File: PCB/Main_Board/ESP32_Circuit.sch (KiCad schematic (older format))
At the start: 24 parts, among them Q1 MBT3904DW1, SW2 EN, SW3 BOOT, U2 ESP32-WROOM-32, U3 FT231XS

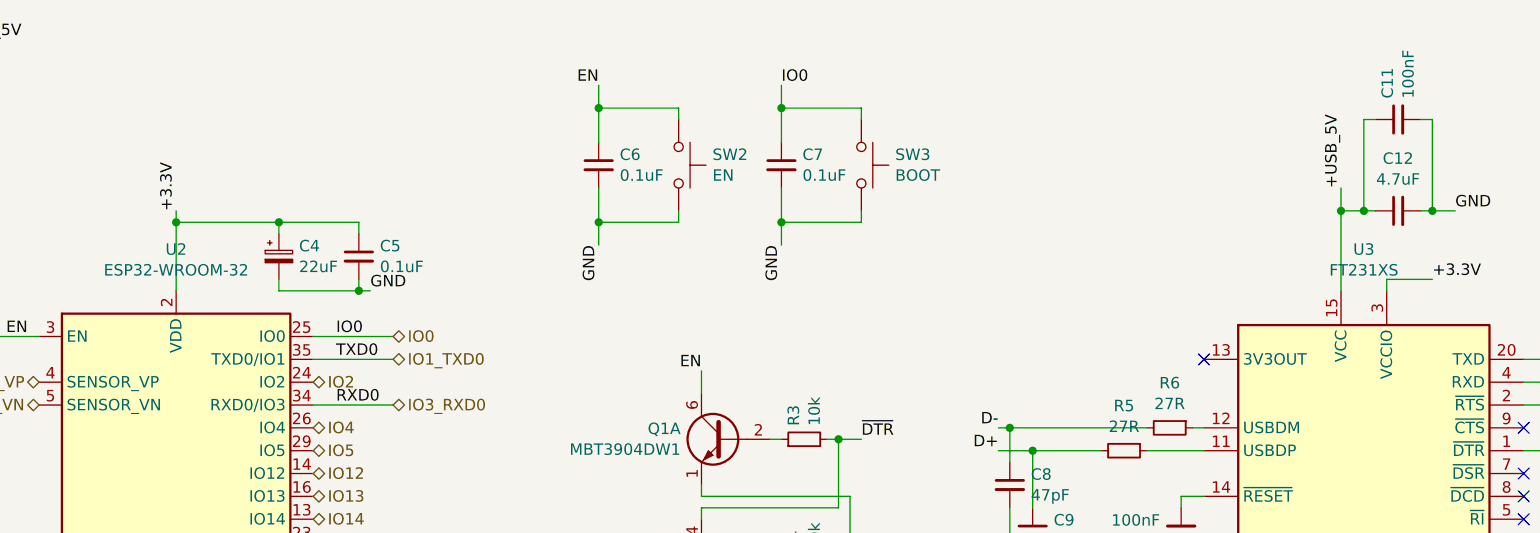
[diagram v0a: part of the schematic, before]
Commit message: Add IR circuit
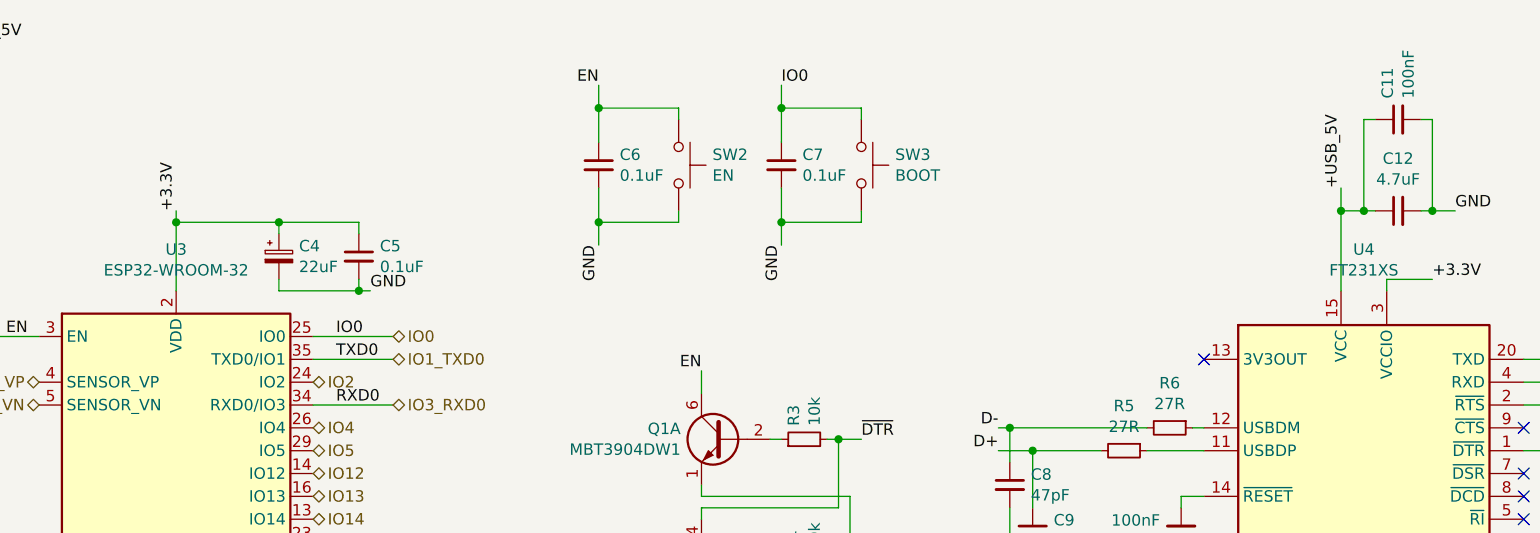
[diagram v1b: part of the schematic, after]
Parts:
- renumbered U2 to U3, U3 to U4
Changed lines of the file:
@@
 AR Path="/5F5D60CE" Ref="U?"  Part="1"
 AR Path="/5F591C5D/5F5D60CE" Ref="U?"  Part="1"
-AR Path="/5F889015/5F5D60CE" Ref="U3"  Part="1"
-F 0 "U3" H 8300 4731 50  0000 C CNN
+AR Path="/5F889015/5F5D60CE" Ref="U4"  Part="1"
+F 0 "U4" H 8300 4731 50  0000 C CNN
 F 1 "FT231XS" H 8300 4640 50  0000 C CNN
 F 2 "Package_SO:SSOP-20_3.9x8.7mm_P0.635mm" H 9300 2850 50  0001 C CNN
@@
 AR Path="/5F5F2511" Ref="U?"  Part="1"
 AR Path="/5F591C5D/5F5F2511" Ref="U?"  Part="1"
-AR Path="/5F889015/5F5F2511" Ref="U2"  Part="1"
-F 0 "U2" H 3100 5731 50  0000 C CNN
+AR Path="/5F889015/5F5F2511" Ref="U3"  Part="1"
+F 0 "U3" H 3100 5731 50  0000 C CNN
 F 1 "ESP32-WROOM-32" H 3100 5640 50  0000 C CNN
 F 2 "RF_Module:ESP32-WROOM-32" H 3100 2650 50  0001 C CNN

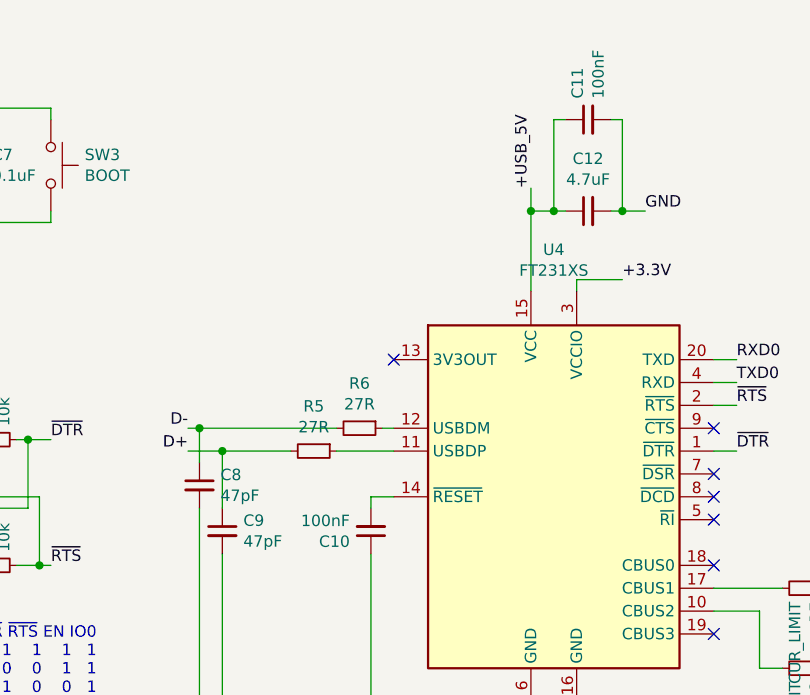
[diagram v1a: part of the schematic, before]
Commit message: Further schematic work and footprint association
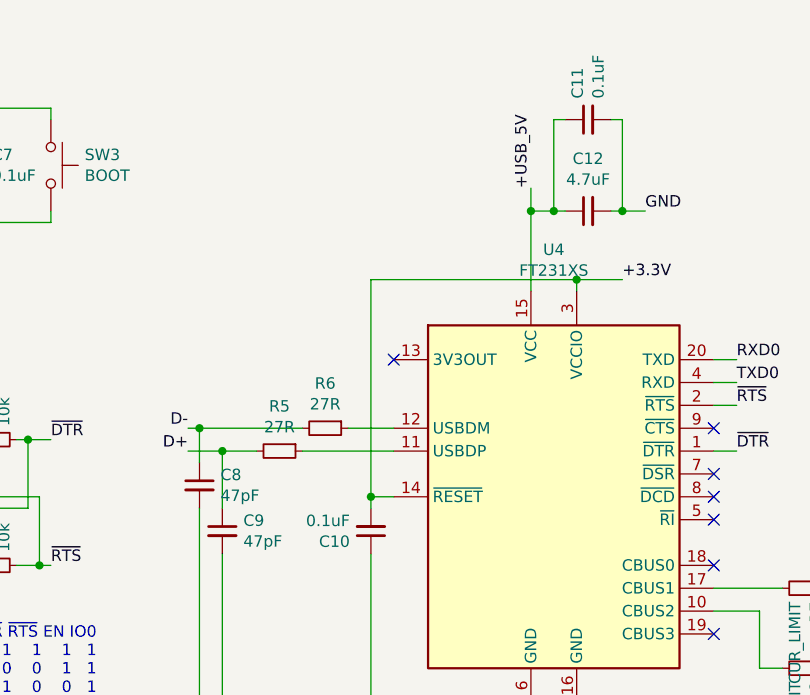
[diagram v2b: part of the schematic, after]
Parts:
- C10, C11: value 100nF -> 0.1uF; footprint (none) -> Capacitor_SMD:C_0603_1608Metric_Pad1.05x0.95mm_HandSolder
- C12, C3, C4, C5, C6, C7, C8, C9: footprint (none) -> Capacitor_SMD:C_0603_1608Metric_Pad1.05x0.95mm_HandSolder
- D5, D6: footprint (none) -> LED_SMD:LED_0603_1608Metric_Pad1.05x0.95mm_HandSolder
- R2, R3, R4, R5, R6, R7, R8: footprint (none) -> Resistor_SMD:R_0603_1608Metric_Pad1.05x0.95mm_HandSolder
- SW2, SW3: footprint (none) -> Button_Switch_THT:SW_PUSH_6mm
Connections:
- net +3.3V: now also C10.2, U4.14 (~RESET)
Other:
- moved on the sheet: R5, R6
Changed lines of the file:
@@
 F 0 "C12" V 8679 2400 50  0000 C CNN
 F 1 "4.7uF" V 8588 2400 50  0000 C CNN
-F 2 "" H 8450 2400 50  0001 C CNN
+F 2 "Capacitor_SMD:C_0603_1608Metric_Pad1.05x0.95mm_HandSolder" H 8450 2400 50  0001 C CNN
 F 3 "~" H 8450 2400 50  0001 C CNN
 	1    8450 2400
@@
 AR Path="/5F889015/5F5D607A" Ref="C11"  Part="1"
 F 0 "C11" H 8542 2046 50  0000 L CNN
-F 1 "100nF" H 8542 1955 50  0000 L CNN
-F 2 "" H 8450 2000 50  0001 C CNN
+F 1 "0.1uF" H 8542 1955 50  0000 L CNN
+F 2 "Capacitor_SMD:C_0603_1608Metric_Pad1.05x0.95mm_HandSolder" H 8450 2000 50  0001 C CNN
 F 3 "~" H 8450 2000 50  0001 C CNN
 	1    8450 2000
@@
 AR Path="/5F889015/5F5D6093" Ref="C10"  Part="1"
 F 0 "C10" H 7592 3846 50  0000 L CNN
-F 1 "100nF" H 7592 3755 50  0000 L CNN
-F 2 "" H 7500 3800 50  0001 C CNN
+F 1 "0.1uF" H 7592 3755 50  0000 L CNN
+F 2 "Capacitor_SMD:C_0603_1608Metric_Pad1.05x0.95mm_HandSolder" H 7500 3800 50  0001 C CNN
 F 3 "~" H 7500 3800 50  0001 C CNN
 	1    7500 3800
@@
 Text Label 6700 3350 2    50   ~ 0
 D-
-$Comp
-L Device:R_Small R?
-U 1 1 5F5D609E
-P 7450 3350
-AR Path="/5F5D609E" Ref="R?"  Part="1"
-AR Path="/5F591C5D/5F5D609E" Ref="R?"  Part="1"
-AR Path="/5F889015/5F5D609E" Ref="R6"  Part="1"
-F 0 "R6" V 7254 3350 50  0000 C CNN
-F 1 "27R" V 7345 3350 50  0000 C CNN
-F 2 "" H 7450 3350 50  0001 C CNN
-F 3 "~" H 7450 3350 50  0001 C CNN
-	1    7450 3350
-	0    1    1    0
-$EndComp
-$Comp
-L Device:R_Small R?
-U 1 1 5F5D60A4
-P 7250 3450
-AR Path="/5F5D60A4" Ref="R?"  Part="1"
-AR Path="/5F591C5D/5F5D60A4" Ref="R?"  Part="1"
-AR Path="/5F889015/5F5D60A4" Ref="R5"  Part="1"
-F 0 "R5" V 7054 3450 50  0000 C CNN
-F 1 "27R" V 7145 3450 50  0000 C CNN
-F 2 "" H 7250 3450 50  0001 C CNN
-F 3 "~" H 7250 3450 50  0001 C CNN
-	1    7250 3450
-	0    1    1    0
-$EndComp
-Wire Wire Line
-	7350 3450 7600 3450
 $Comp
 L Device:C_Small C?
@@
 F 0 "C8" H 6842 3646 50  0000 L CNN
 F 1 "47pF" H 6842 3555 50  0000 L CNN
-F 2 "" H 6750 3600 50  0001 C CNN
+F 2 "Capacitor_SMD:C_0603_1608Metric_Pad1.05x0.95mm_HandSolder" H 6750 3600 50  0001 C CNN
 F 3 "~" H 6750 3600 50  0001 C CNN
 	1    6750 3600
@@
 F 0 "C9" H 6942 3846 50  0000 L CNN
 F 1 "47pF" H 6942 3755 50  0000 L CNN
-F 2 "" H 6850 3800 50  0001 C CNN
+F 2 "Capacitor_SMD:C_0603_1608Metric_Pad1.05x0.95mm_HandSolder" H 6850 3800 50  0001 C CNN
 F 3 "~" H 6850 3800 50  0001 C CNN
 	1    6850 3800
@@
 Wire Wire Line
 	6750 3500 6750 3350
-Connection ~ 6750 3350
-Wire Wire Line
-	6750 3350 7350 3350
 Wire Wire Line
 	6850 3700 6850 3450
-Connection ~ 6850 3450
-Wire Wire Line
-	6850 3450 7150 3450
-Wire Wire Line
-	7550 3350 7600 3350
 Wire Wire Line
 	6750 4600 6850 4600
@@
 F 0 "D6" H 9650 4635 50  0000 C CNN
 F 1 "TX_LED" H 9650 4544 50  0000 C CNN
-F 2 "" V 9650 4400 50  0001 C CNN
+F 2 "LED_SMD:LED_0603_1608Metric_Pad1.05x0.95mm_HandSolder" V 9650 4400 50  0001 C CNN
 F 3 "~" V 9650 4400 50  0001 C CNN
 	1    9650 4400
@@
 F 0 "R8" H 9459 4446 50  0000 L CNN
 F 1 "CUR_LIMIT" H 9459 4355 50  0000 L CNN
-F 2 "" H 9400 4400 50  0001 C CNN
+F 2 "Resistor_SMD:R_0603_1608Metric_Pad1.05x0.95mm_HandSolder" H 9400 4400 50  0001 C CNN
 F 3 "~" H 9400 4400 50  0001 C CNN
 	1    9400 4400
@@
 F 0 "D5" H 9650 4285 50  0000 C CNN
 F 1 "RX_LED" H 9650 4194 50  0000 C CNN
-F 2 "" V 9650 4050 50  0001 C CNN
+F 2 "LED_SMD:LED_0603_1608Metric_Pad1.05x0.95mm_HandSolder" V 9650 4050 50  0001 C CNN
 F 3 "~" V 9650 4050 50  0001 C CNN
 	1    9650 4050
@@
 F 0 "R7" H 9459 4096 50  0000 L CNN
 F 1 "CUR_LIMIT" H 9459 4005 50  0000 L CNN
-F 2 "" H 9400 4050 50  0001 C CNN
+F 2 "Resistor_SMD:R_0603_1608Metric_Pad1.05x0.95mm_HandSolder" H 9400 4050 50  0001 C CNN
 F 3 "~" H 9400 4050 50  0001 C CNN
 	1    9400 4050
@@
 F 0 "C4" H 3638 2646 50  0000 L CNN
 F 1 "22uF" H 3638 2555 50  0000 L CNN
-F 2 "" H 3550 2600 50  0001 C CNN
+F 2 "Capacitor_SMD:C_0603_1608Metric_Pad1.05x0.95mm_HandSolder" H 3550 2600 50  0001 C CNN
 F 3 "~" H 3550 2600 50  0001 C CNN
 	1    3550 2600
@@
 F 0 "C5" H 3992 2646 50  0000 L CNN
 F 1 "0.1uF" H 3992 2555 50  0000 L CNN
-F 2 "" H 3900 2600 50  0001 C CNN
+F 2 "Capacitor_SMD:C_0603_1608Metric_Pad1.05x0.95mm_HandSolder" H 3900 2600 50  0001 C CNN
 F 3 "~" H 3900 2600 50  0001 C CNN
 	1    3900 2600
@@
 F 0 "C3" H 2042 3146 50  0000 L CNN
 F 1 "0.1uF" H 2042 3055 50  0000 L CNN
-F 2 "" H 1950 3100 50  0001 C CNN
+F 2 "Capacitor_SMD:C_0603_1608Metric_Pad1.05x0.95mm_HandSolder" H 1950 3100 50  0001 C CNN
 F 3 "~" H 1950 3100 50  0001 C CNN
 	1    1950 3100
@@
 F 0 "C6" H 5042 2246 50  0000 L CNN
 F 1 "0.1uF" H 5042 2155 50  0000 L CNN
-F 2 "" H 4950 2200 50  0001 C CNN
+F 2 "Capacitor_SMD:C_0603_1608Metric_Pad1.05x0.95mm_HandSolder" H 4950 2200 50  0001 C CNN
 F 3 "~" H 4950 2200 50  0001 C CNN
 	1    4950 2200
@@
 F 0 "SW2" V 5254 2348 50  0000 L CNN
 F 1 "EN" V 5345 2348 50  0000 L CNN
-F 2 "" H 5300 2400 50  0001 C CNN
+F 2 "Button_Switch_THT:SW_PUSH_6mm" H 5300 2400 50  0001 C CNN
 F 3 "~" H 5300 2400 50  0001 C CNN
 	1    5300 2200
@@
 F 0 "C7" H 5842 2246 50  0000 L CNN
 F 1 "0.1uF" H 5842 2155 50  0000 L CNN
-F 2 "" H 5750 2200 50  0001 C CNN
+F 2 "Capacitor_SMD:C_0603_1608Metric_Pad1.05x0.95mm_HandSolder" H 5750 2200 50  0001 C CNN
 F 3 "~" H 5750 2200 50  0001 C CNN
 	1    5750 2200
@@
 F 0 "SW3" V 6054 2348 50  0000 L CNN
 F 1 "BOOT" V 6145 2348 50  0000 L CNN
-F 2 "" H 6100 2400 50  0001 C CNN
+F 2 "Button_Switch_THT:SW_PUSH_6mm" H 6100 2400 50  0001 C CNN
 F 3 "~" H 6100 2400 50  0001 C CNN
 	1    6100 2200
@@
 F 0 "R3" H 5909 3446 50  0000 L CNN
 F 1 "10k" H 5909 3355 50  0000 L CNN
-F 2 "" H 5850 3400 50  0001 C CNN
+F 2 "Resistor_SMD:R_0603_1608Metric_Pad1.05x0.95mm_HandSolder" H 5850 3400 50  0001 C CNN
 F 3 "~" H 5850 3400 50  0001 C CNN
 	1    5850 3400
@@
 F 0 "R4" H 5909 3996 50  0000 L CNN
 F 1 "10k" H 5909 3905 50  0000 L CNN
-F 2 "" H 5850 3950 50  0001 C CNN
+F 2 "Resistor_SMD:R_0603_1608Metric_Pad1.05x0.95mm_HandSolder" H 5850 3950 50  0001 C CNN
 F 3 "~" H 5850 3950 50  0001 C CNN
 	1    5850 3950
@@
 F 0 "R2" H 1891 2754 50  0000 R CNN
 F 1 "10k" H 1891 2845 50  0000 R CNN
-F 2 "" H 1950 2800 50  0001 C CNN
+F 2 "Resistor_SMD:R_0603_1608Metric_Pad1.05x0.95mm_HandSolder" H 1950 2800 50  0001 C CNN
 F 3 "~" H 1950 2800 50  0001 C CNN
 	1    1950 2800
@@
 Text HLabel 4050 3050 2    50   BiDi ~ 0
 IO1_TXD0
+$Comp
+L Device:R_Small R?
+U 1 1 5F5D60A4
+P 7100 3450
+AR Path="/5F5D60A4" Ref="R?"  Part="1"
+AR Path="/5F591C5D/5F5D60A4" Ref="R?"  Part="1"
+AR Path="/5F889015/5F5D60A4" Ref="R5"  Part="1"
+F 0 "R5" V 6904 3450 50  0000 C CNN
+F 1 "27R" V 6995 3450 50  0000 C CNN
+F 2 "Resistor_SMD:R_0603_1608Metric_Pad1.05x0.95mm_HandSolder" H 7100 3450 50  0001 C CNN
+F 3 "~" H 7100 3450 50  0001 C CNN
+	1    7100 3450
+	0    1    1    0
+$EndComp
+$Comp
+L Device:R_Small R?
+U 1 1 5F5D609E
+P 7300 3350
+AR Path="/5F5D609E" Ref="R?"  Part="1"
+AR Path="/5F591C5D/5F5D609E" Ref="R?"  Part="1"
+AR Path="/5F889015/5F5D609E" Ref="R6"  Part="1"
+F 0 "R6" V 7104 3350 50  0000 C CNN
+F 1 "27R" V 7195 3350 50  0000 C CNN
+F 2 "Resistor_SMD:R_0603_1608Metric_Pad1.05x0.95mm_HandSolder" H 7300 3350 50  0001 C CNN
+F 3 "~" H 7300 3350 50  0001 C CNN
+	1    7300 3350
+	0    1    1    0
+$EndComp
+Wire Wire Line
+	6750 3350 7200 3350
+Connection ~ 6750 3350
+Wire Wire Line
+	7000 3450 6850 3450
+Connection ~ 6850 3450
+Wire Wire Line
+	7400 3350 7600 3350
+Wire Wire Line
+	7200 3450 7600 3450
+Wire Wire Line
+	7500 3650 7500 2700
+Wire Wire Line
+	7500 2700 8400 2700
+Connection ~ 7500 3650
+Connection ~ 8400 2700
 $EndSCHEMATC

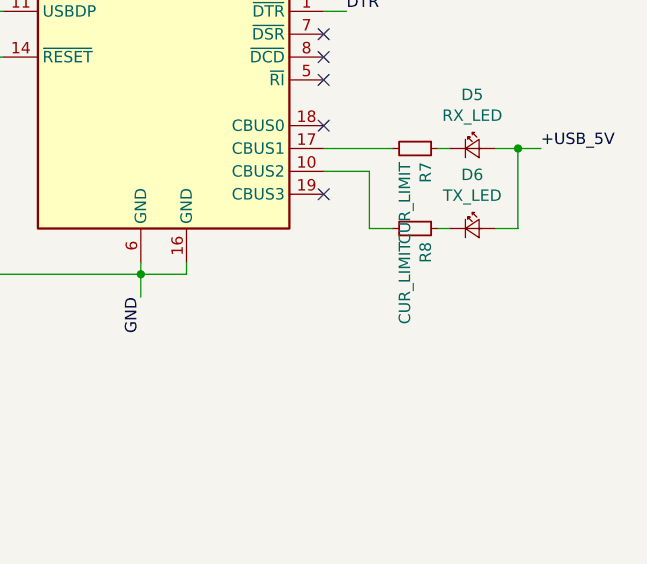
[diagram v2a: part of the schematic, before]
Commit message: Further sourcing on mouser
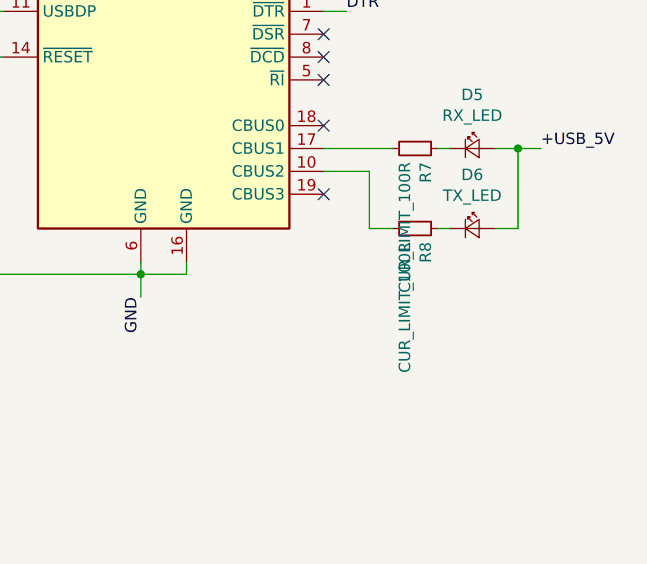
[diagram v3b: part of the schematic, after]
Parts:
- R7, R8: value CUR_LIMIT -> CUR_LIMIT_100R
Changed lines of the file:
@@
 AR Path="/5F889015/5F5D60DB" Ref="R8"  Part="1"
 F 0 "R8" H 9459 4446 50  0000 L CNN
-F 1 "CUR_LIMIT" H 9459 4355 50  0000 L CNN
+F 1 "CUR_LIMIT_100R" H 9459 4355 50  0000 L CNN
 F 2 "Resistor_SMD:R_0603_1608Metric_Pad1.05x0.95mm_HandSolder" H 9400 4400 50  0001 C CNN
 F 3 "~" H 9400 4400 50  0001 C CNN
@@
 AR Path="/5F889015/5F5D60E8" Ref="R7"  Part="1"
 F 0 "R7" H 9459 4096 50  0000 L CNN
-F 1 "CUR_LIMIT" H 9459 4005 50  0000 L CNN
+F 1 "CUR_LIMIT_100R" H 9459 4005 50  0000 L CNN
 F 2 "Resistor_SMD:R_0603_1608Metric_Pad1.05x0.95mm_HandSolder" H 9400 4050 50  0001 C CNN
 F 3 "~" H 9400 4050 50  0001 C CNN

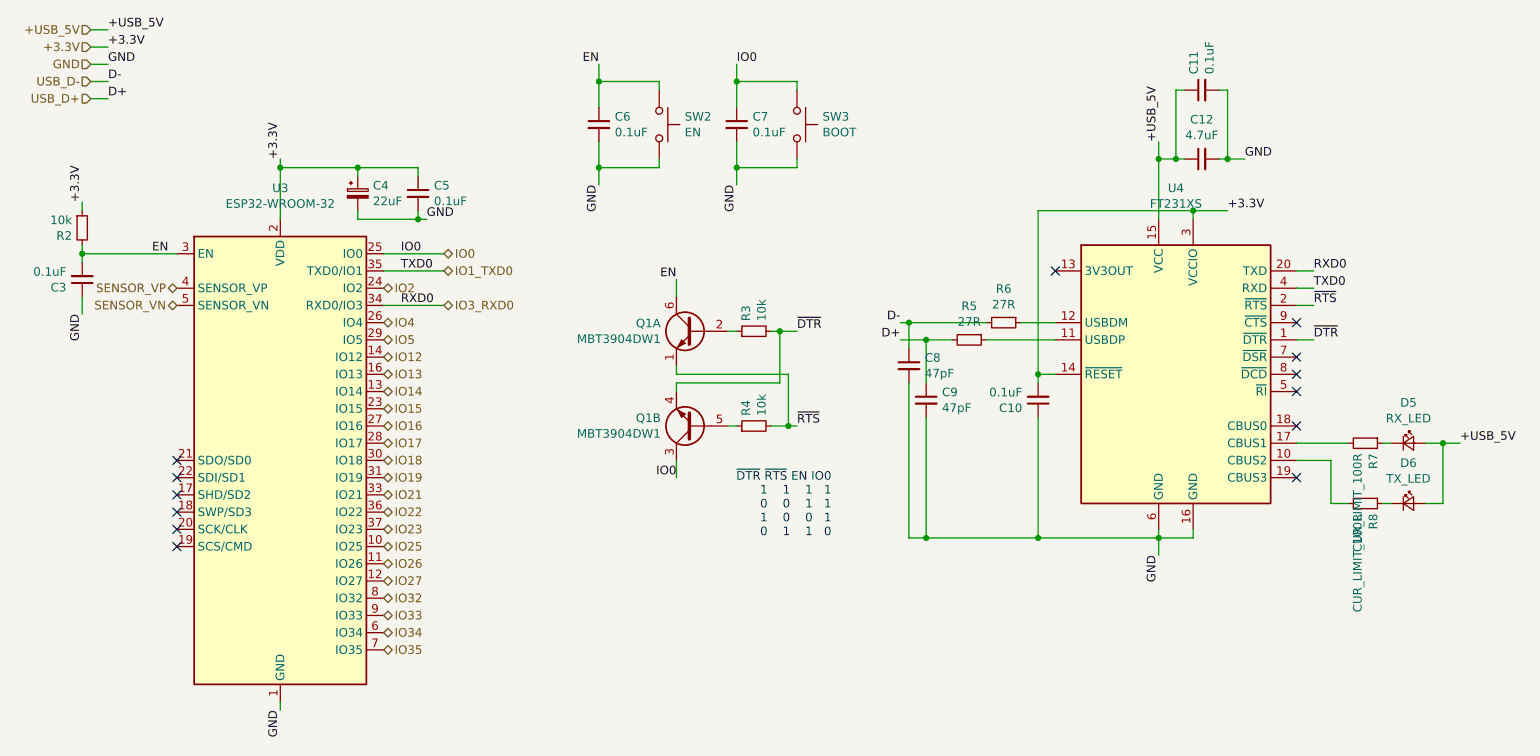
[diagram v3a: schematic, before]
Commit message: Add level shifter and further PCB work
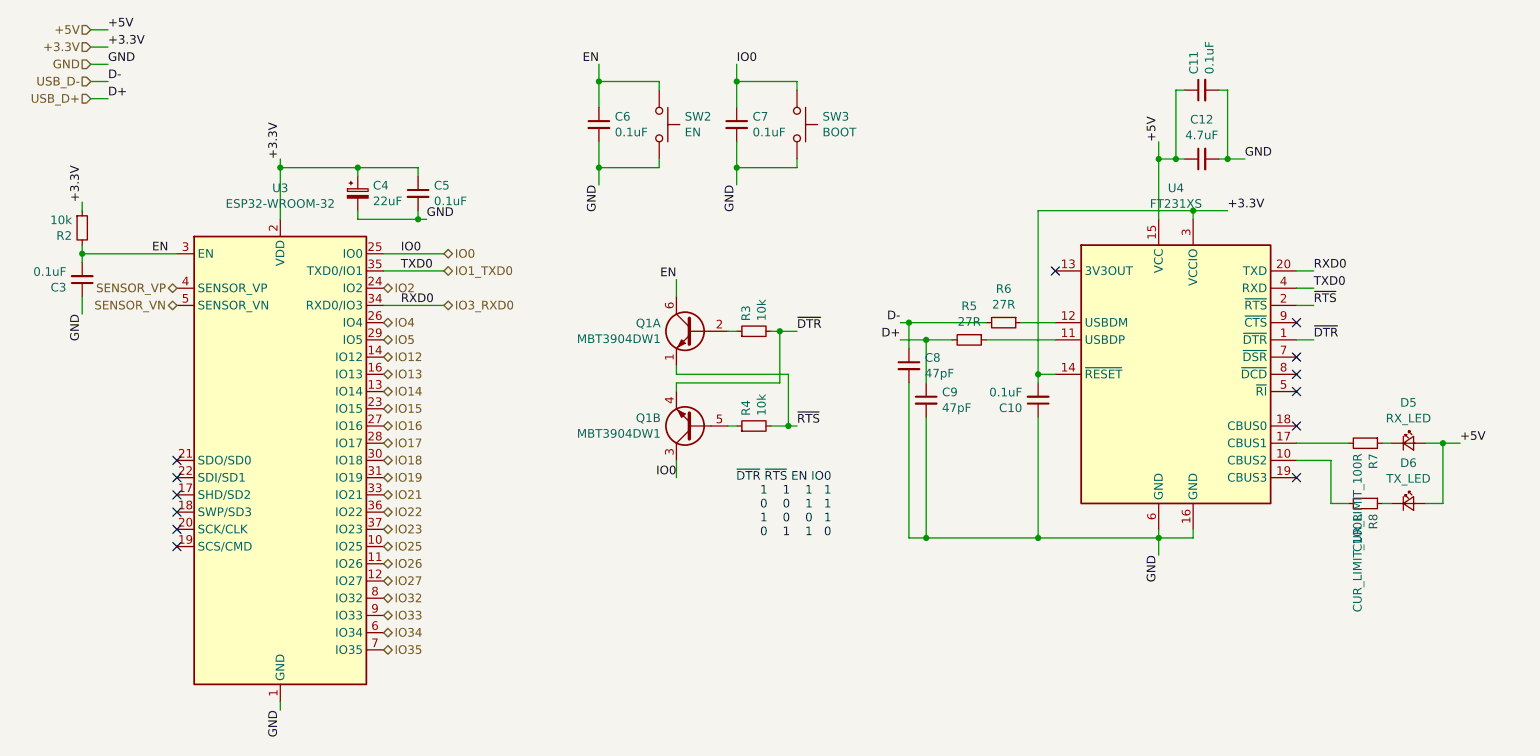
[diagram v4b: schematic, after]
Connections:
- net +USB_5V renamed +5V
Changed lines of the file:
@@
 	8600 2400 8700 2400
 Text HLabel 2000 1650 0    50   Input ~ 0
-+USB_5V
++5V
 Text HLabel 2000 1850 0    50   Input ~ 0
 GND
 Text Label 2100 1650 0    50   ~ 0
-+USB_5V
++5V
 Text Label 2100 1850 0    50   ~ 0
 GND
@@
 GND
 Text Label 9950 4050 0    50   ~ 0
-+USB_5V
++5V
 Text Label 8200 2300 1    50   ~ 0
-+USB_5V
++5V
 Text Label 8600 2700 0    50   ~ 0
 +3.3V

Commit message: Change buttons, make board more compact, add extra mounting hole
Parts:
- SW2, SW3: footprint Button_Switch_THT:SW_PUSH_6mm -> SamacSys:SKTHAHE010
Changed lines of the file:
@@
 Sheet 2 4
 Title "ESP32 Programming Circuit"
-Date "2020-09-08"
+Date "2020-09-10"
 Rev "v1.0"
 Comp "Richard Carter"
@@
 F 0 "SW2" V 5254 2348 50  0000 L CNN
 F 1 "EN" V 5345 2348 50  0000 L CNN
-F 2 "Button_Switch_THT:SW_PUSH_6mm" H 5300 2400 50  0001 C CNN
+F 2 "SamacSys:SKTHAHE010" H 5300 2400 50  0001 C CNN
 F 3 "~" H 5300 2400 50  0001 C CNN
 	1    5300 2200
@@
 F 0 "SW3" V 6054 2348 50  0000 L CNN
 F 1 "BOOT" V 6145 2348 50  0000 L CNN
-F 2 "Button_Switch_THT:SW_PUSH_6mm" H 6100 2400 50  0001 C CNN
+F 2 "SamacSys:SKTHAHE010" H 6100 2400 50  0001 C CNN
 F 3 "~" H 6100 2400 50  0001 C CNN
 	1    6100 2200
